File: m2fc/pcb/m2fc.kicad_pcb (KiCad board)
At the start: 4 copper layers, 100 x 70 mm, 350 parts, among them IC101 ADP3335, IC102 STM32F405VGT, IC103 ADP3335, IC201 AD8226, IC202 AD8656, IC203 AD8541, IC204 AD8226, IC205 AD8656, IC206 AD8541, IC207 AD8226, IC208 AD8656, IC209 AD8541, IC301 ADXL375, IC302 ADXL345, IC303 MS5611-01BA03, IC304 HMC5883L, IC305 L3G4200D, IC401 ADuM5201, IC402 ADuM1201, IC601 AD8495, IC602 AD8656, IC603 AD8495, IC604 AD8656, IC605 AD8495, IC606 AD8656, P101 CONN_2, P102 CONN_2, P103 CONN_2, P104 SWD, P201 CONN_4, P202 CONN_4, P203 CONN_4, P401 CONN_4, P402 CONN_2, P403 CONN_4, P501 CONN_2, P502 CONN_2, P503 CONN_2, P601 CONN_2, P602 CONN_2, P603 CONN_2, Q501 MOSFET_P, Q502 MOSFET_N, Q503 MOSFET_P, Q504 MOSFET_N, Q505 MOSFET_P, Q506 MOSFET_N, U106 MICROSD, U107 MOUNT, U108 MOUNT, U109 MOUNT, U110 MOUNT, U111 MOUNT, U112 MOUNT, X101 8M

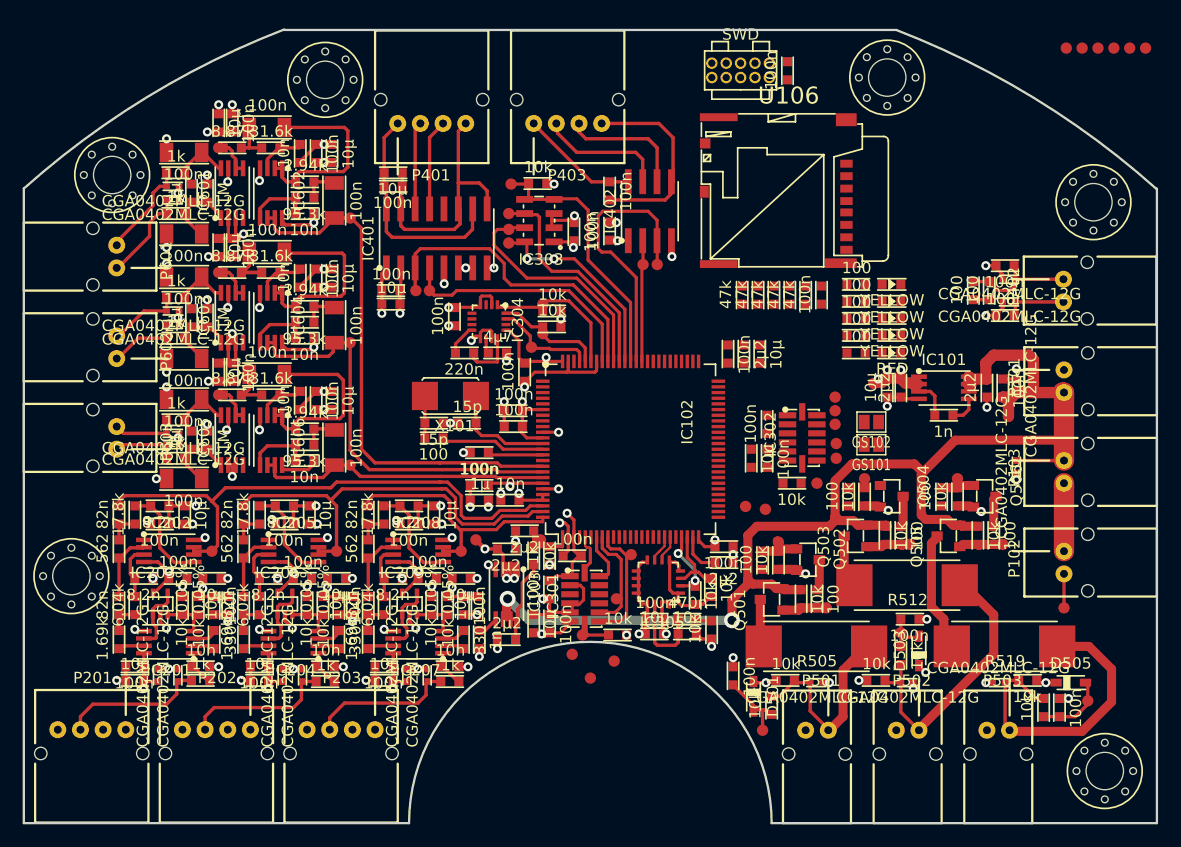
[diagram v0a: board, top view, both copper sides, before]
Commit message: routing intensifies
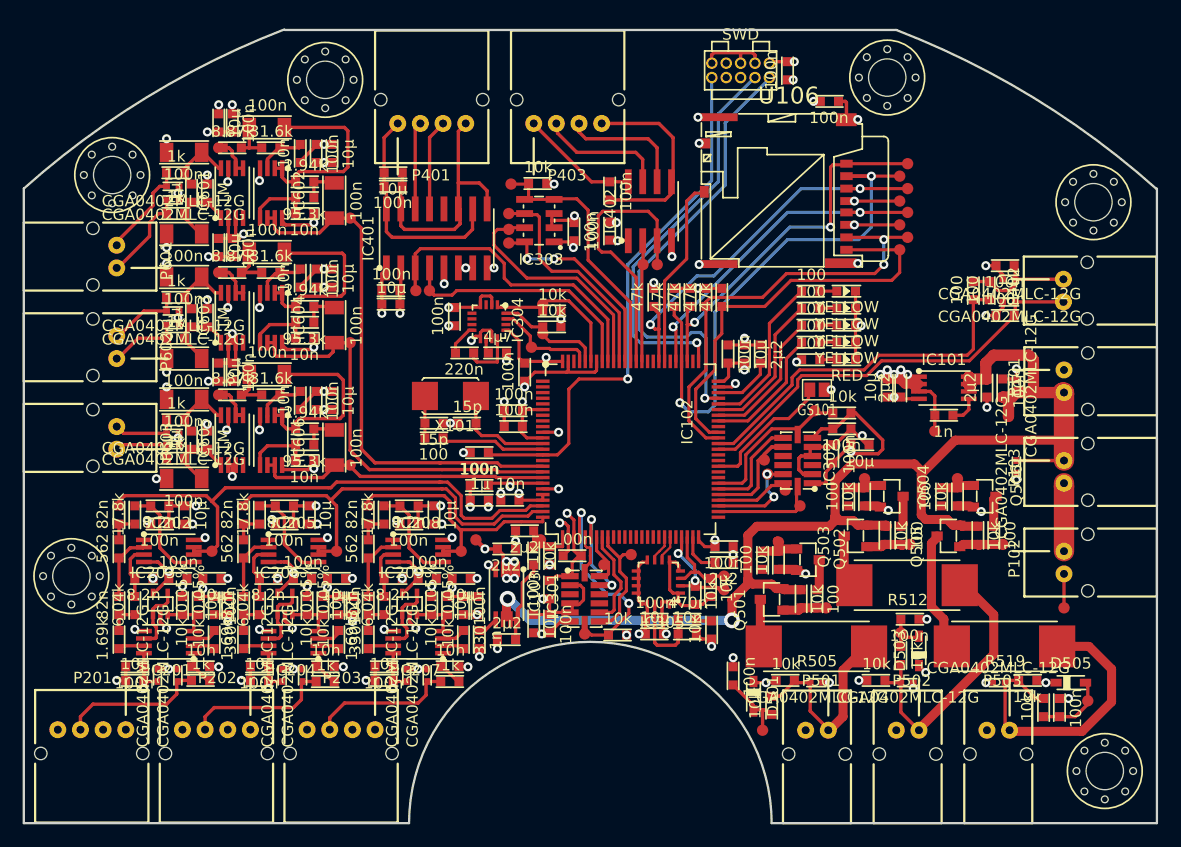
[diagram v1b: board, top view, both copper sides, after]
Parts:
- removed GS102: GS2, Connect:GS2
- removed TP302, TP303, TP307, TP311: TESTPAD, m2fc:TESTPAD
- added TP113: TESTPAD, m2fc:TESTPAD, F.Cu at (127.3, 45.1)
- added TP114: TESTPAD, m2fc:TESTPAD, F.Cu at (127.3, 47.2)
- moved TP106 28.1 mm to (127.3, 49.4)
- moved TP105 25.7 mm to (128.0, 48.3)
- moved TP110 23.3 mm to (128.0, 46.1)
- moved TP109 20.9 mm to (128.0, 44.0)
- moved TP108 19.7 mm to (127.3, 42.9)
- moved TP107 17.3 mm to (128.0, 41.8)
- moved C108 16.3 mm to (120.3, 36.3), turned to 0 degrees
- moved TP312 10.1 mm to (118.5, 72.0)
- moved C306 9.02 mm to (123.0, 66.6), turned to 0 degrees
- moved R302 8.63 mm to (123.0, 63.8), turned to 180 degrees
- moved TP309 8.38 mm to (101.2, 77.2)
- moved TP310 8.27 mm to (117.2, 70.6)
- moved TP313 7.98 mm to (111.8, 79.4)
- moved R107 7.80 mm to (105.6, 52.8)
- moved R104 7.40 mm to (111.6, 52.8)
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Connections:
- IC102 pad 51: /IMU/LG_ACCEL_CS -> Net-(IC102-Pad51)
- IC102 pad 55: /IMU/LG_ACCEL_INT1 -> /IMU/LG_ACCEL_INT2
- IC102 pad 56: /IMU/LG_ACCEL_INT2 -> /IMU/LG_ACCEL_INT1
- IC102 pad 57: Net-(IC102-Pad57) -> /IMU/LG_ACCEL_CS
- IC102 pad 61: /SJ2 -> Net-(IC102-Pad61)
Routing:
- net /SD_DAT3: track 0.00 -> 49.0 mm, vias 0 -> 2
- net GND: track 194.9 -> 238.8 mm, vias 96 -> 109
- net /nRST: track 4.94 -> 47.7 mm, vias 0 -> 1
- net /SWDIO: track 0.00 -> 40.0 mm, vias 0 -> 1
- net /SD_DAT0: track 0.00 -> 39.7 mm, vias 0 -> 2
- net +3.3V: track 90.4 -> 128.0 mm, vias 22 -> 32
- net /SD_DAT1: track 0.00 -> 37.0 mm
- net /SD_CMD: track 0.00 -> 36.2 mm, vias 0 -> 2
- net /SWCLK: track 0.00 -> 34.8 mm, vias 0 -> 1
- net /SD_DAT2: track 0.00 -> 33.6 mm, vias 0 -> 2
- net /IO/LED_C: track 5.77 -> 37.2 mm
- net /SD_CLK: track 0.00 -> 30.7 mm, vias 0 -> 2
- net /IO/LED_A: track 1.40 -> 32.1 mm
- net /SD_CD: track 0.00 -> 16.9 mm
- net /IMU/HG_ACCEL_CS: track 3.03 -> 19.0 mm, vias 0 -> 2
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
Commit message: nc 0
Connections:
- IC102 pad 39: /Pyros/PYRO_1_F -> /Pyros/PYRO_2_C
- IC102 pad 40: /Pyros/PYRO_2_C -> /Pyros/PYRO_3_C
- IC102 pad 41: /Pyros/PYRO_2_F -> /Pyros/PYRO_1_F
- IC102 pad 42: /Pyros/PYRO_3_C -> /Pyros/PYRO_2_F
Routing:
- net /Pyros/PYRO_3_C: track 6.59 -> 61.6 mm, vias 0 -> 2
- net /Pyros/PYRO_2_C: track 4.51 -> 39.8 mm, vias 0 -> 2
- net /Pyros/PYRO_3_F: track 0.00 -> 27.8 mm, vias 0 -> 2
- net /Pyros/PYRO_1_C: track 6.65 -> 32.7 mm, vias 0 -> 2
- net /Pyros/PYRO_1_F: track 0.00 -> 23.1 mm, vias 0 -> 2
- net /Pyros/PYRO_2_F: track 0.00 -> 20.1 mm, vias 0 -> 2

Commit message: tidied up
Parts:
- moved C122 7.42 mm to (82.4, 64.8), turned to 270 degrees
- moved TP104 4.73 mm to (136.4, 59.4)
- moved C102 1.60 mm to (136.4, 60.8), turned to 270 degrees
- moved D102 1.20 mm to (137.6, 60.8), turned to 270 degrees
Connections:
- P101 pad 1: GND -> +BATT
- P101 pad 2: +BATT -> GND
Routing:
- net GND: track 238.8 -> 554.2 mm, vias 109 -> 200
- net /nRST: track 47.7 -> 81.3 mm, vias 1 -> 0
- net /Pyros/PYRO_1_F: track 23.1 -> 20.0 mm
- net +BATT: track 124.7 -> 123.1 mm
- net /Pyros/PYRO_3_C: track 61.6 -> 60.3 mm
- net /SWDIO: track 40.0 -> 40.9 mm
- net (no net): track 0.60 -> 0.00 mm
- net /SWCLK: track 34.8 -> 35.4 mm
- added copper zone on B.Cu, net GND
- added copper zone on F.Cu, net GND

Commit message: more tidying
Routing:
- net GND: track 554.2 -> 524.0 mm, vias 200 -> 190
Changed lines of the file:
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@@
     (thickness 1.6)
     (drawings 9)
-    (tracks 2591)
+    (tracks 2570)
     (zones 0)
     (modules 347)
@@
   )
   (setup
-    (last_trace_width 0.4)
+    (last_trace_width 0.3)
     (user_trace_width 0.2)
     (user_trace_width 0.28)
@@
   (segment (start 120 33) (end 120 32) (width 0.5) (layer F.Cu) (net 1))
   (segment (start 118.6 34.4) (end 120 33) (width 0.5) (layer F.Cu) (net 1))
-  (segment (start 110.72 32.72) (end 110 32) (width 0.5) (layer B.Cu) (net 1))
-  (via (at 82 34) (size 0.8) (drill 0.4) (layers F.Cu B.Cu) (net 1))
-  (segment (start 85 34) (end 82 34) (width 0.5) (layer F.Cu) (net 1))
-  (via (at 85 34) (size 0.8) (drill 0.4) (layers F.Cu B.Cu) (net 1))
-  (segment (start 88 34) (end 85 34) (width 0.5) (layer B.Cu) (net 1))
-  (via (at 88 34) (size 0.8) (drill 0.4) (layers F.Cu B.Cu) (net 1))
-  (segment (start 91 34) (end 88 34) (width 0.5) (layer F.Cu) (net 1))
-  (via (at 91 34) (size 0.8) (drill 0.4) (layers F.Cu B.Cu) (net 1))
-  (segment (start 94 34) (end 91 34) (width 0.5) (layer B.Cu) (net 1))
-  (via (at 94 34) (size 0.8) (drill 0.4) (layers F.Cu B.Cu) (net 1))
-  (segment (start 97 34) (end 94 34) (width 0.5) (layer F.Cu) (net 1))
-  (via (at 97 34) (size 0.8) (drill 0.4) (layers F.Cu B.Cu) (net 1))
-  (segment (start 100 34) (end 97 34) (width 0.5) (layer B.Cu) (net 1))
-  (via (at 100 34) (size 0.8) (drill 0.4) (layers F.Cu B.Cu) (net 1))
-  (segment (start 103 34) (end 100 34) (width 0.5) (layer F.Cu) (net 1))
-  (via (at 103 34) (size 0.8) (drill 0.4) (layers F.Cu B.Cu) (net 1))
-  (segment (start 106 34) (end 103 34) (width 0.5) (layer B.Cu) (net 1))
-  (via (at 106 34) (size 0.8) (drill 0.4) (layers F.Cu B.Cu) (net 1))
-  (segment (start 109 34) (end 106 34) (width 0.5) (layer F.Cu) (net 1))
-  (via (at 109 34) (size 0.8) (drill 0.4) (layers F.Cu B.Cu) (net 1))
-  (segment (start 110 32) (end 109 34) (width 0.5) (layer B.Cu) (net 1))
   (via (at 66.8 35) (size 0.8) (drill 0.4) (layers F.Cu B.Cu) (net 1))
   (segment (start 62.6 38.4) (end 62.35 37.75) (width 0.5) (layer F.Cu) (net 1))
@@
   (segment (start 107.3 39.5) (end 107.3 43.4) (width 0.3) (layer F.Cu) (net 41))
   (segment (start 101 38.25) (end 106.05 38.25) (width 0.3) (layer F.Cu) (net 41))
+  (segment (start 95 38.25) (end 95 39.1) (width 0.3) (layer F.Cu) (net 42))
+  (segment (start 99.3 43.4) (end 101.7 43.4) (width 0.3) (layer F.Cu) (net 42))
+  (segment (start 95 39.1) (end 99.3 43.4) (width 0.3) (layer F.Cu) (net 42))
   (segment (start 103.4 43.4) (end 103.35 43.393) (width 0.3) (layer F.Cu) (net 42))
   (segment (start 101.7 43.4) (end 103.4 43.4) (width 0.3) (layer F.Cu) (net 42))
-  (segment (start 94.9 38.2) (end 95 38.25) (width 0.3) (layer F.Cu) (net 42))
-  (segment (start 100.1 43.4) (end 94.9 38.2) (width 0.3) (layer F.Cu) (net 42))
-  (segment (start 101.7 43.4) (end 100.1 43.4) (width 0.3) (layer F.Cu) (net 42))
   (segment (start 113.6 81.7) (end 113.6 87.1) (width 0.28) (layer B.Cu) (net 43))
   (segment (start 103.3 79.4) (end 104.9 81) (width 0.28) (layer B.Cu) (net 43))
@@
   (segment (start 99 38.3) (end 99 38.25) (width 0.3) (layer F.Cu) (net 175))
   (segment (start 99 39) (end 99 38.3) (width 0.3) (layer F.Cu) (net 175))
-  (segment (start 105.89 40.39) (end 105.1 39.6) (width 0.3) (layer F.Cu) (net 175))
-  (segment (start 105.1 39.6) (end 99.6 39.6) (width 0.3) (layer F.Cu) (net 175))
-  (segment (start 99.6 39.6) (end 99 39) (width 0.3) (layer F.Cu) (net 175))
+  (segment (start 105.89 40.39) (end 105.5 40) (width 0.3) (layer F.Cu) (net 175))
+  (segment (start 105.5 40) (end 100 40) (width 0.3) (layer F.Cu) (net 175))
+  (segment (start 100 40) (end 99 39) (width 0.3) (layer F.Cu) (net 175))
   (segment (start 105.89 43.393) (end 105.89 40.39) (width 0.3) (layer F.Cu) (net 175))
   (segment (start 97.1 38.3) (end 97 38.25) (width 0.3) (layer F.Cu) (net 176))
-  (segment (start 104.62 41.42) (end 104 40.8) (width 0.3) (layer F.Cu) (net 176))
-  (segment (start 104 40.8) (end 98.8 40.8) (width 0.3) (layer F.Cu) (net 176))
-  (segment (start 98.8 40.8) (end 97.1 39.1) (width 0.3) (layer F.Cu) (net 176))
+  (segment (start 104.62 41.42) (end 104.2 41) (width 0.3) (layer F.Cu) (net 176))
+  (segment (start 104.2 41) (end 99 41) (width 0.3) (layer F.Cu) (net 176))
+  (segment (start 99 41) (end 97.1 39.1) (width 0.3) (layer F.Cu) (net 176))
   (segment (start 97.1 39.1) (end 97.1 38.3) (width 0.3) (layer F.Cu) (net 176))
   (segment (start 104.62 43.393) (end 104.62 41.42) (width 0.3) (layer F.Cu) (net 176))
@@
       )
     )
+    (polygon
+      (pts        (xy 93.2 57.9) (xy 93.2 53.6) (xy 88.9 53.6) (xy 88.9 57.9)
+      )
+    )
+    (polygon
+      (pts        (xy 108 47.5) (xy 108 33) (xy 80.5 33) (xy 80.5 47.5)
+      )
+    )

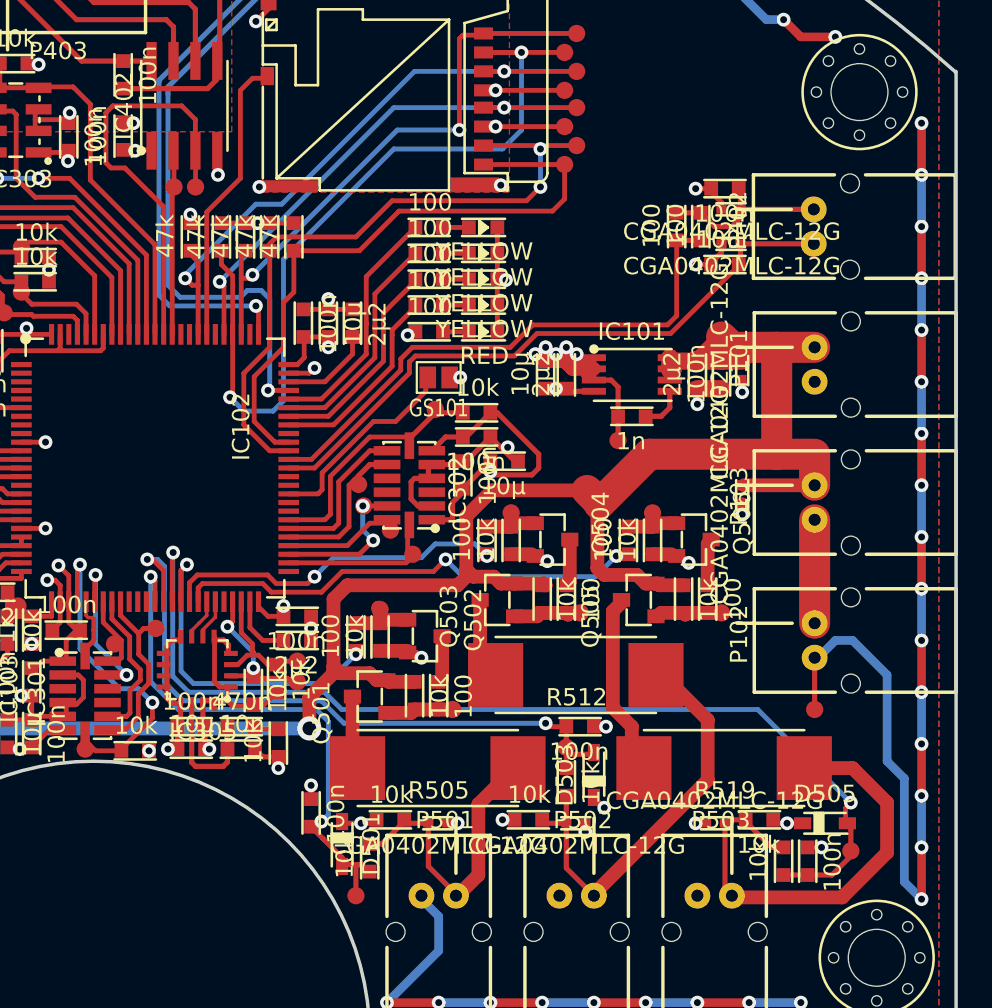
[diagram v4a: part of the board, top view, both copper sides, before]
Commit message: flip around power connectors
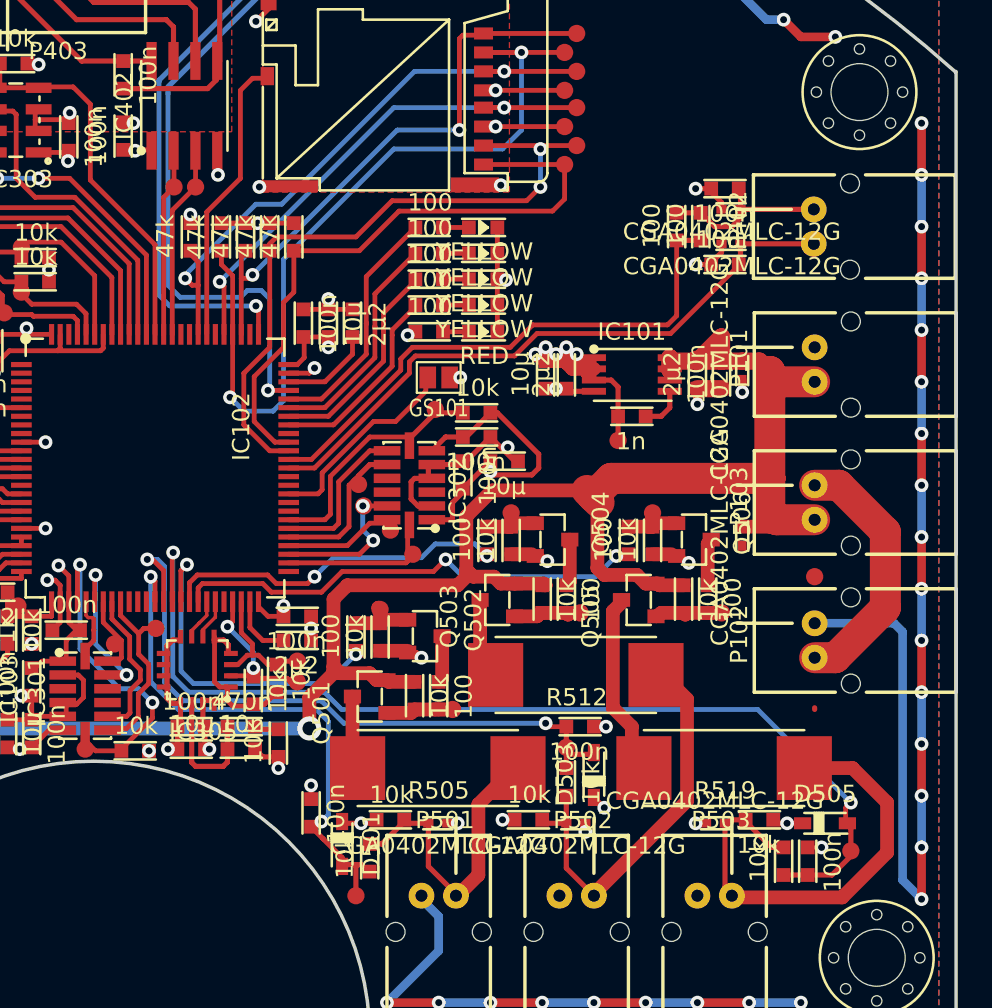
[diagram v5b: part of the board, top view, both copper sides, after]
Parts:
- moved TP103 7.70 mm to (141.8, 73.3)
- moved D101 2.40 mm to (137.6, 70.4)
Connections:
- IC402 pad 2: /IO/SER_OUT_2 -> /IO/SER_IN_2
- IC402 pad 3: /IO/SER_IN_2 -> /IO/SER_OUT_2
- P101 pad 1: +BATT -> GND
- P101 pad 2: GND -> +BATT
- P102 pad 1: Net-(P102-Pad1) -> GND
- P102 pad 2: GND -> Net-(P102-Pad2)
- P103 pad 1: +BATT -> Net-(P102-Pad2)
- P103 pad 2: Net-(P102-Pad1) -> +BATT
- TP403 pad 1: /IO/SER_OUT_2 -> /IO/SER_IN_2
- TP404 pad 1: /IO/SER_IN_2 -> /IO/SER_OUT_2
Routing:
- net Net-(P102-Pad2): track 0.00 -> 15.1 mm
- net /IO/SER_IN_2: track 24.5 -> 11.1 mm
- net Net-(P102-Pad1): track 6.00 -> 0.00 mm
- net GND: track 524.0 -> 522.4 mm, vias 190 -> 189
- net Net-(D504-Pad1): track 25.7 -> 24.7 mm
- net /IO/SER_OUT_2: track 10.7 -> 11.4 mm

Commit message: done?
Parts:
- added G***: LOGO, m2fc:cusf_logo_full, B.Cu at (93.0, 59.5)
- moved TP604 1.78 mm to (77.4, 58.7)
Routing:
- net GND: track 522.4 -> 516.3 mm, vias 189 -> 191
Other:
- board text added: "+ -"
- board text added: "1"
- board text added: "2"
- board text added: "3"
- board text added: "3V DIGITAL"
- board text added: "3V3 TX RX GND"
- board text added: "A C"
- board text added: "ADAM GREIG 2014-07-31"
- board text added: "ARM"
- board text added: "AUX"
- board text added: "BAT"
- board text added: "BODY NOSE"
- board text added: "EXCITE SIGNAL GROUND SHIELD"
- board text added: "FLIGHT MODE:"
- board text added: "GREEN WHITE"
- board text added: "GYRO"
- board text added: "HG ACCEL"
- board text added: "LED"
- board text added: "LG ACCEL"
- board text added: "MAGNO"
- board text added: "MARTLET 2 FLIGHT COMPUTER"
- board text added: "MASTER SERIAL"
- board text added: "PRYOS"
- board text added: "PYRO 1"
- board text added: "PYRO 2"
- board text added: "PYRO 3"
- board text added: "SD CARD"
- board text added: "SENSORS"
- board text added: "SLAVE SERIAL"
- board text added: "STATUS"
- board text added: "STRAIN GAUGE"
- board text added: "THERMO COUPLE"
- board text added: "VISO RX TX GND"
- board text added: "X"
- board text added: "Y"
- board text added: "Z"
- board text added: "cusf.co.uk"
- board text added: "r1"
